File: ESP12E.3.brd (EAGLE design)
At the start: 16.8 x 32.5 mm, 24 parts, among them SW1 PTS840-GP-SMTR-LFS, U1 SPX3819M5-L-3-3

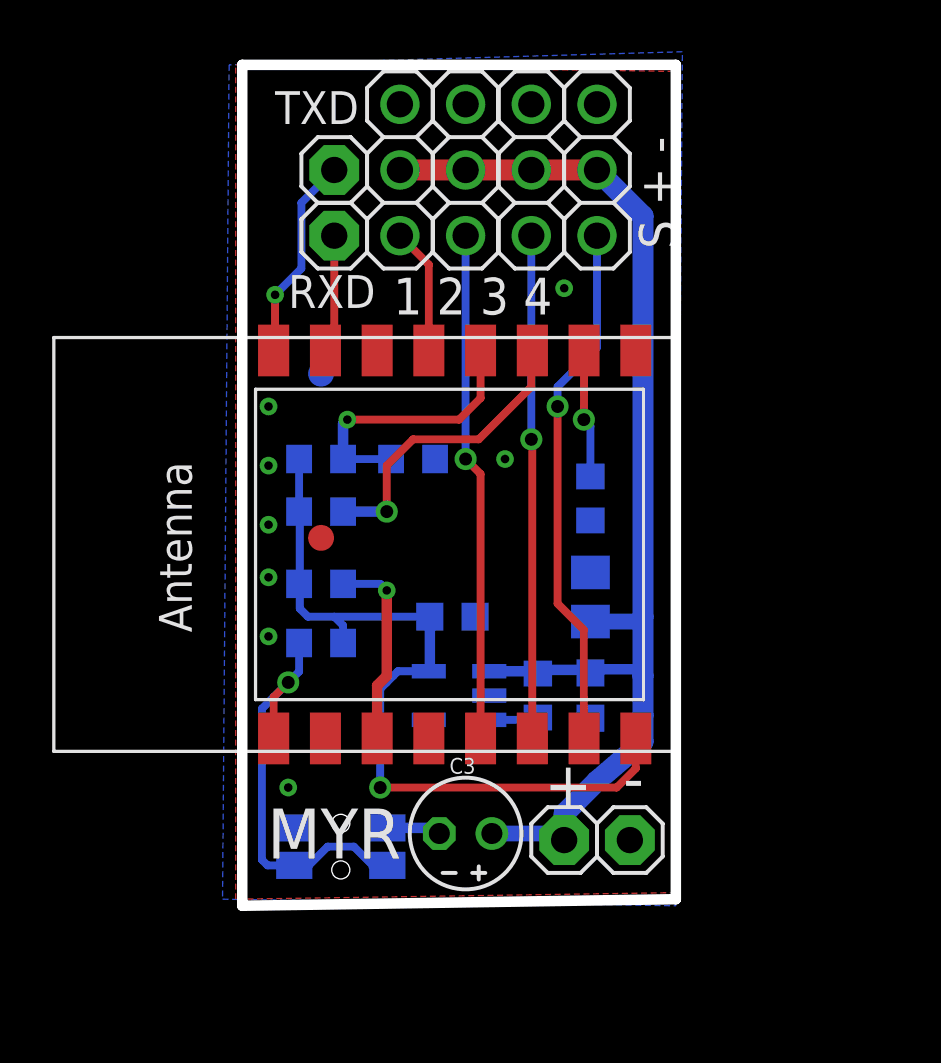
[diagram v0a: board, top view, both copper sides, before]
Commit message: New Programming Header
Modified loading method with 6 pin header.
Flipped board in layout as most parts were on bottom layer.
Board power now matches 3 pin servo cable.
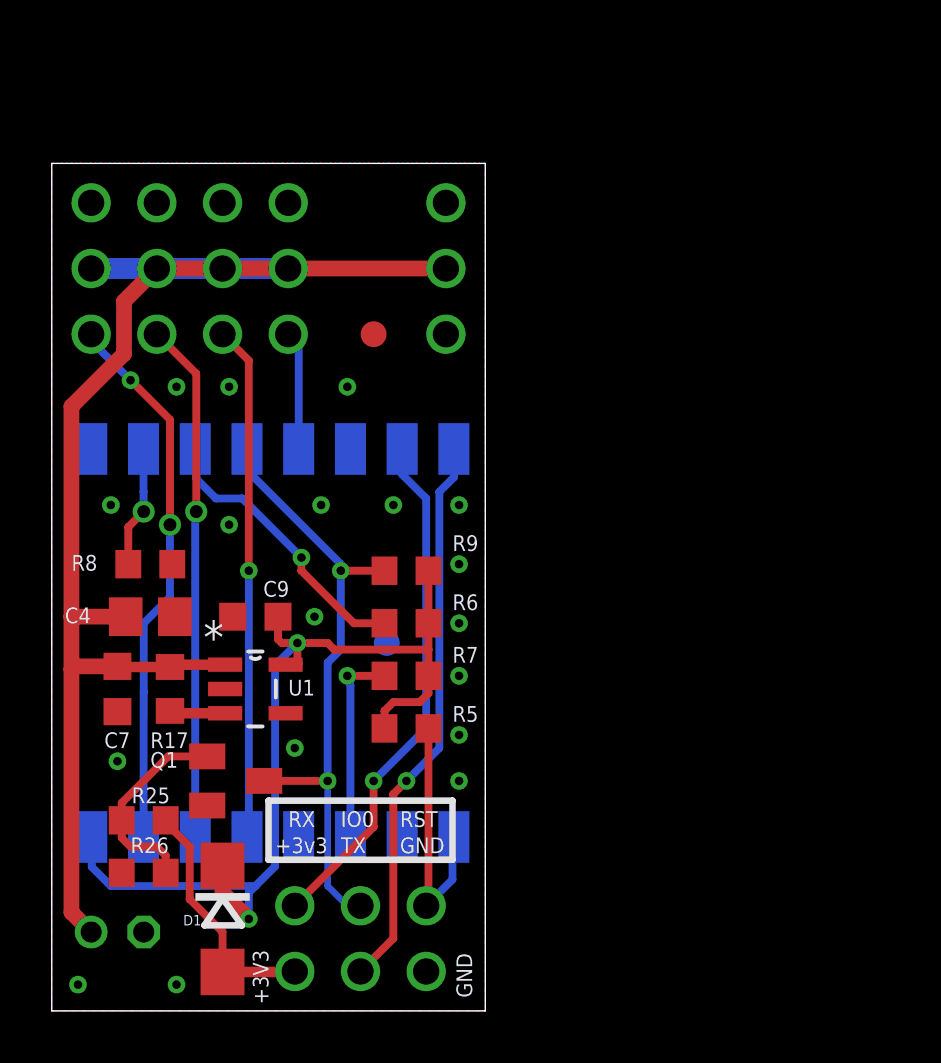
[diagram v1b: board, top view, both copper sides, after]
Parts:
- removed R1: DNP, adafruit:R0603
- removed RXD, RXD1, TXD, TXD1: (no value), adafruit:1X01
- removed SW1: PTS840-GP-SMTR-LFS, PTS840-G_P-SMTR-LFS:PTS840-G*P-SMTR-LFS
- added D1: (no value), diode:DO214AC
- added JP10, JP11, JP9: (no value), adafruit:1X03
- added Q1: (no value), adafruit:SOT23
- added R25, R26: 10k, adafruit:R0603
- moved JP4 19.9 mm to (1.52, 28.7), flipped to the bottom
- moved C7 18.3 mm to (2.54, 12.4), flipped to the top
- moved R8 17.2 mm to (3.81, 17.3), flipped to the top, turned to 180 degrees
- moved C4 17.0 mm to (3.81, 15.2), flipped to the top, turned to 0 degrees
- moved JP3 15.0 mm to (4.06, 28.7), flipped to the bottom
- moved R17 14.2 mm to (4.57, 12.4), flipped to the top
- moved C3 14.0 mm to (2.54, 3.05), flipped to the bottom
- moved JP2 10.1 mm to (6.60, 28.7), flipped to the bottom
- moved U1 7.88 mm to (7.87, 12.4), flipped to the top
- moved C9 7.62 mm to (7.87, 15.2), flipped to the top
- moved JP1 5.76 mm to (9.14, 28.7), flipped to the bottom
- moved R6 5.44 mm to (13.7, 15.0), flipped to the top
- moved R9 5.44 mm to (13.7, 17.0), flipped to the top
- moved R7 4.85 mm to (13.7, 13.0), flipped to the top
- moved U$3 4.79 mm to (13.0, 14.2), flipped to the bottom
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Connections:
- new net N$7: Q1.1, R25.1, R26.2
- new net P3V3: D1.A, JP11.1, R25.2
- net +3V3: now also D1.C
- net GND: now also JP10.1, JP10.3, JP11.3, Q1.2, R26.1; no longer R1.1, RXD1.1, SW1.1, SW1.2
- net GPIO0: now also JP9.2, Q1.3; no longer R1.2
- net RESET: now also JP9.3; no longer SW1.3, SW1.4
- net RXD: now also JP9.1; no longer RXD.1
- net TXD: now also JP11.2; no longer TXD.1
- net VMOT: now also JP10.2; no longer TXD1.1
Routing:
- net RXD: track 4.70 -> 20.8 mm, vias 0 -> 1
- net TXD: track 7.95 -> 21.8 mm
- net GPIO0: track 10.8 -> 24.4 mm, vias 1 -> 2
- net P3V3: track 0.00 -> 9.71 mm
- net N$7: track 0.00 -> 8.06 mm
- net VMOT: track 47.3 -> 54.5 mm
- net RESET: track 16.9 -> 10.00 mm, vias 1 -> 0
- net +3V3: track 32.5 -> 39.2 mm, vias 1 -> 2
- net GND: track 2.10 -> 0.35 mm, vias 8 -> 18
- net GPIO12: track 19.5 -> 20.5 mm
- net GPIO2: track 11.7 -> 11.1 mm
- net GPIO13: track 20.5 -> 21.1 mm, vias 1 -> 2
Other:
- board size 16.8 x 32.5 mm -> 16.8 x 32.8 mm
- board text added: "+ -"
- board text added: "+3V3"
- board text added: "+3v3"
- board text added: "C4"
- board text added: "GND"
- board text added: "IO0"
- board text added: "R8"
- board text added: "RST"
- board text added: "RX"
- board text added: "TX"
- board text removed: "+"
- board text removed: "-"
- board text removed: "MYR"

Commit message: License Update
Licensed under CERN OHL v.1.2 or later
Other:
- board text added: "Project located at: https://github.com/OpenMYR/ESP12E.3/ Copyright Christopher Adams 2016. Licensed under CERN OHL v.1.2 or later This documentation is distributed WITHOUT ANY EXPRESS OR IMPLIED WARRANTY, INCLUDING OF MERCHANTABILITY, SATISFACTORY QUALITY AND FITNESS FOR A PARTICULAR PURPOSE. Please see the CERN OHL v.1.2 for applicable conditions"
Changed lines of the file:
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@@
 <text x="0.508" y="14.986" size="0.6096" layer="21">C4</text>
 <text x="0.762" y="17.018" size="0.6096" layer="21">R8</text>
+<text x="30.988" y="-0.508" size="1.778" layer="48">Project located at:
+https://github.com/OpenMYR/ESP12E.3/
+Copyright Christopher Adams 2016.
+Licensed under CERN OHL v.1.2 or later
+This documentation is distributed WITHOUT
+ANY EXPRESS OR IMPLIED WARRANTY,
+INCLUDING OF MERCHANTABILITY,
+SATISFACTORY QUALITY AND FITNESS
+FOR A PARTICULAR PURPOSE.
+Please see the CERN OHL v.1.2 for applicable conditions</text>
 </plain>
 <attributes>
@@
 </board>
 </drawing>
+<compatibility>
+<note version="6.3" minversion="6.2.2" severity="warning">
+Since Version 6.2.2 text objects can contain more than one line,
+which will not be processed correctly with this version.
+</note>
+</compatibility>
 </eagle>

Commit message: //Increased board size and added M3 mounting holes
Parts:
- added H1, H2, H3, H4: MOUNT-HOLE3.6, holes:3,6
- added LOGO1: OSHW-LOGOMINI, SparkFun-Aesthetics:OSHW-LOGO-MINI
- moved C3 8.05 mm to (10.5, 3.94)
- moved C7 8.05 mm to (10.5, 13.3)
- moved C9 8.05 mm to (15.9, 16.1)
- moved D1 8.05 mm to (14.6, 4.45)
- moved JP2 8.05 mm to (14.6, 29.6)
- moved JP4 8.05 mm to (9.53, 29.6)
- moved R17 8.05 mm to (12.6, 13.3)
- moved R25 8.05 mm to (11.6, 8.26)
- moved R26 8.05 mm to (11.6, 6.22)
- moved U1 8.05 mm to (15.9, 13.3)
- moved X1 8.05 mm to (19.1, 15.1)
- moved C4 8.05 mm to (11.8, 16.1)
- moved JP1 8.05 mm to (17.1, 29.6)
- moved JP10 8.05 mm to (23.2, 29.6)
- moved JP11 8.05 mm to (19.9, 2.41)
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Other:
- board size 16.8 x 32.8 mm -> 32.4 x 33.7 mm
- board text added: "ESP12"
- board text added: "MYR"
- board text added: "Open"
- board text added: "WIFI SERVO DRIVER"
